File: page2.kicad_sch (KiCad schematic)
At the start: 74 parts, among them SW28 SRBV141404

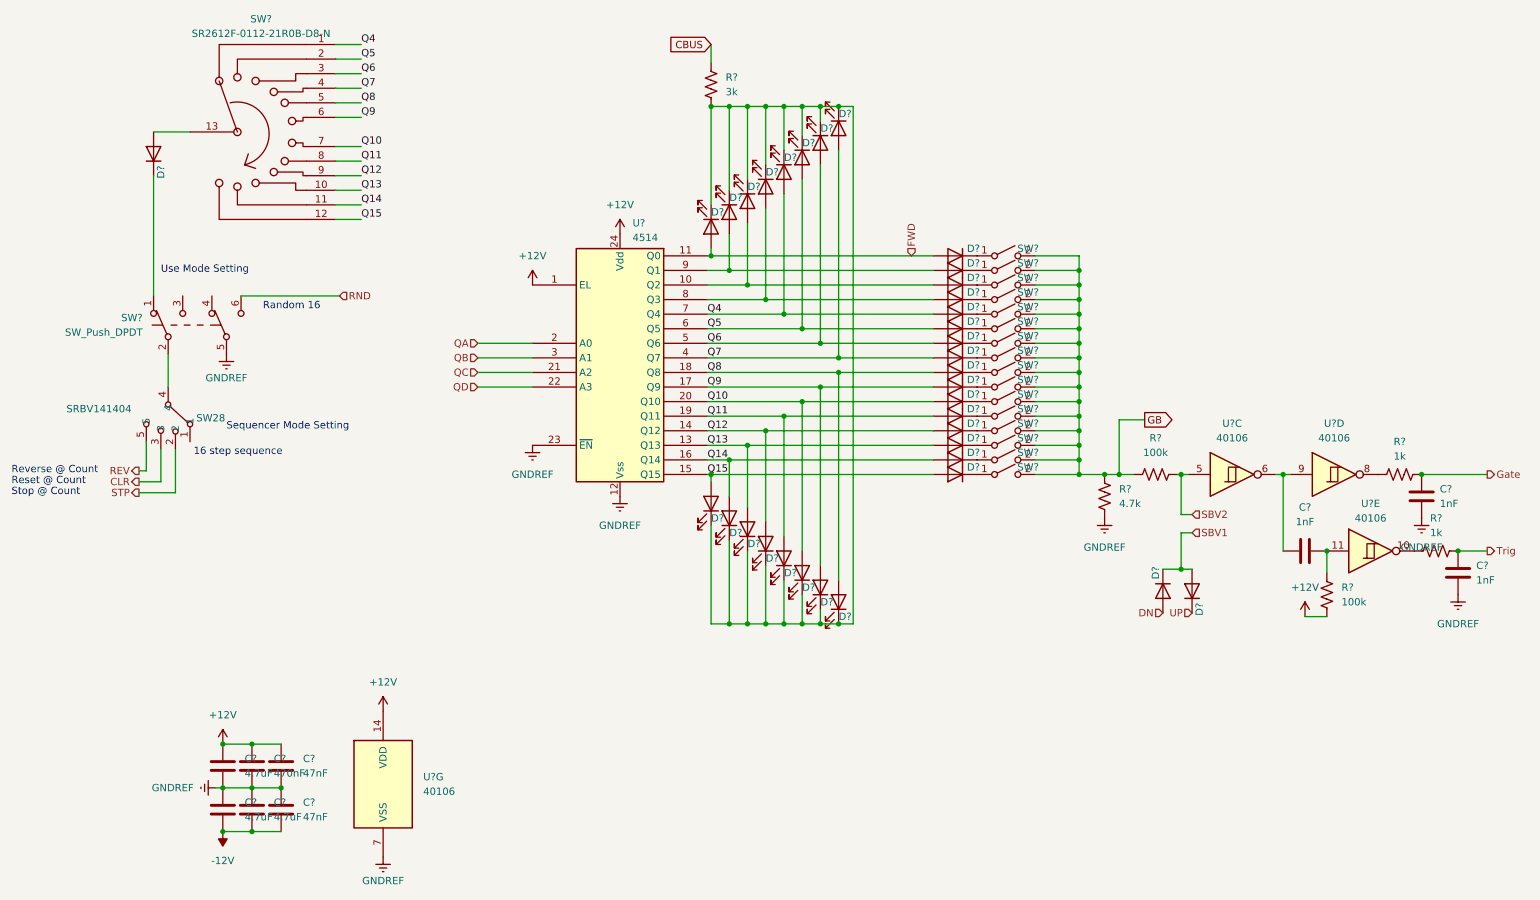
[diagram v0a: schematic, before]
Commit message: created pcb file, placed parts
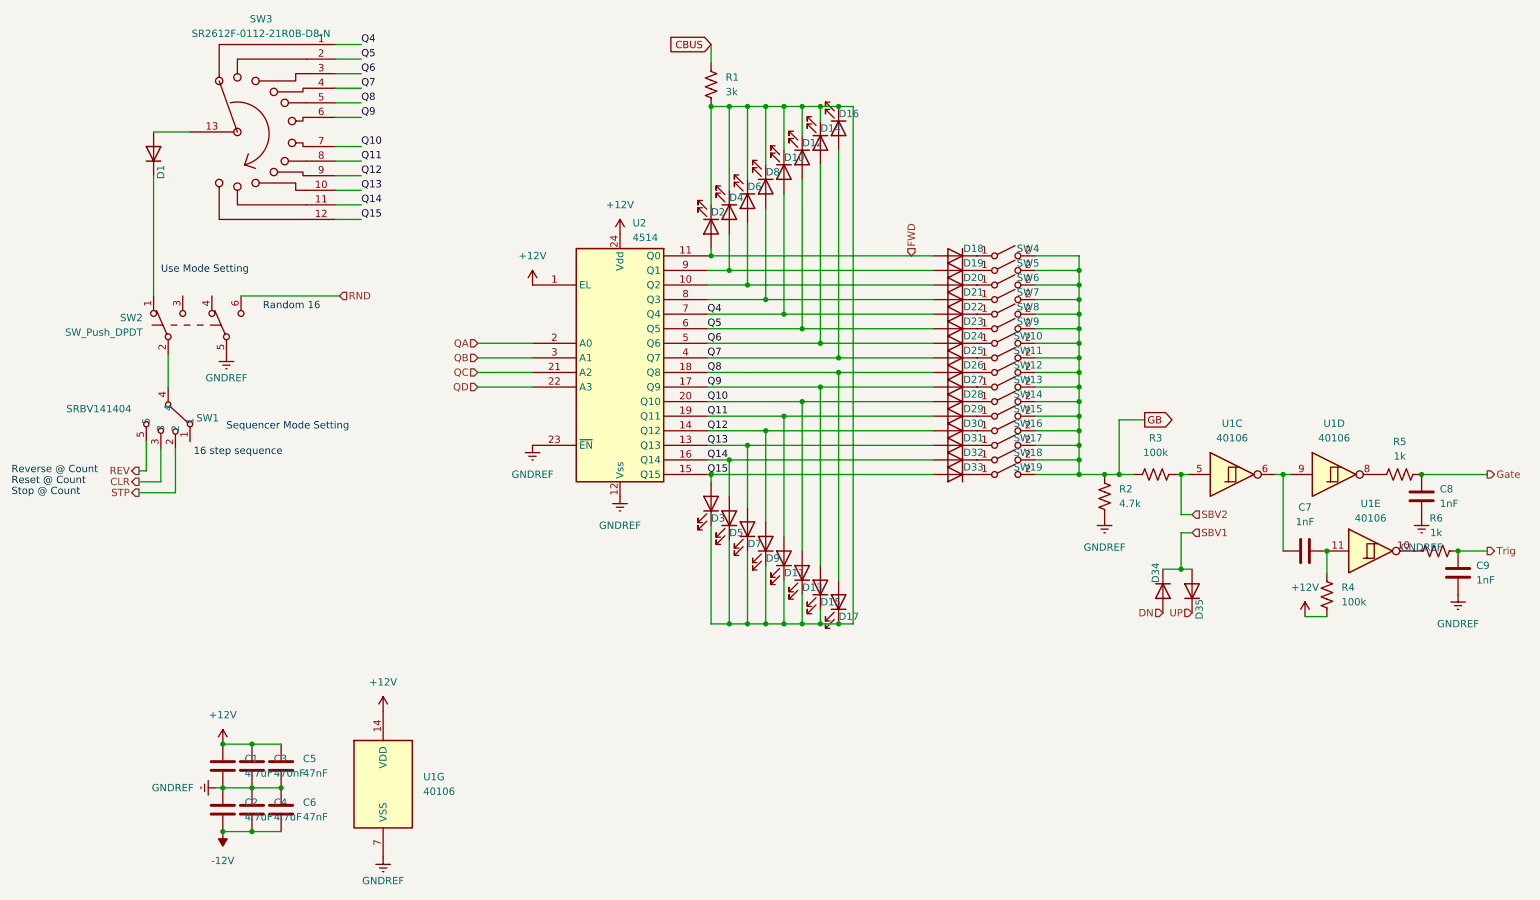
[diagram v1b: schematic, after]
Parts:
- gave numbers to parts that had none: 70
- renumbered SW28 to SW1

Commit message: routing and placing
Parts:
- D10, D11, D12, D13, D14, D15, D16, D17, D2, D3, D4, D5, D6, D7, D8, D9: footprint LED_SMD:LED_0805_2012Metric -> LED_THT:LED_D5.0mm
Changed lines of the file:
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@@
       (effects (font (size 1.27 1.27)) (justify left) hide)
     )
-    (property "Footprint" "LED_SMD:LED_0805_2012Metric" (at 140.97 109.22 0)
+    (property "Footprint" "LED_THT:LED_D5.0mm" (at 140.97 109.22 0)
       (effects (font (size 1.27 1.27)) hide)
     )
@@
       (effects (font (size 1.27 1.27)) (justify left) hide)
     )
-    (property "Footprint" "LED_SMD:LED_0805_2012Metric" (at 137.795 53.975 0)
+    (property "Footprint" "LED_THT:LED_D5.0mm" (at 137.795 53.975 0)
       (effects (font (size 1.27 1.27)) hide)
     )
@@
       (effects (font (size 1.27 1.27)) (justify left) hide)
     )
-    (property "Footprint" "LED_SMD:LED_0805_2012Metric" (at 147.32 114.3 0)
+    (property "Footprint" "LED_THT:LED_D5.0mm" (at 147.32 114.3 0)
       (effects (font (size 1.27 1.27)) hide)
     )
@@
       (effects (font (size 1.27 1.27)) (justify left) hide)
     )
-    (property "Footprint" "LED_SMD:LED_0805_2012Metric" (at 150.495 44.45 0)
+    (property "Footprint" "LED_THT:LED_D5.0mm" (at 150.495 44.45 0)
       (effects (font (size 1.27 1.27)) hide)
     )
@@
       (effects (font (size 1.27 1.27)) (justify left) hide)
     )
-    (property "Footprint" "LED_SMD:LED_0805_2012Metric" (at 153.67 119.38 0)
+    (property "Footprint" "LED_THT:LED_D5.0mm" (at 153.67 119.38 0)
       (effects (font (size 1.27 1.27)) hide)
     )
@@
       (effects (font (size 1.27 1.27)) (justify left) hide)
     )
-    (property "Footprint" "LED_SMD:LED_0805_2012Metric" (at 144.145 111.76 0)
+    (property "Footprint" "LED_THT:LED_D5.0mm" (at 144.145 111.76 0)
       (effects (font (size 1.27 1.27)) hide)
     )
@@
       (effects (font (size 1.27 1.27)) (justify left) hide)
     )
-    (property "Footprint" "LED_SMD:LED_0805_2012Metric" (at 153.67 41.91 0)
+    (property "Footprint" "LED_THT:LED_D5.0mm" (at 153.67 41.91 0)
       (effects (font (size 1.27 1.27)) hide)
     )
@@
       (effects (font (size 1.27 1.27)) (justify left) hide)
     )
-    (property "Footprint" "LED_SMD:LED_0805_2012Metric" (at 140.97 52.07 0)
+    (property "Footprint" "LED_THT:LED_D5.0mm" (at 140.97 52.07 0)
       (effects (font (size 1.27 1.27)) hide)
     )
@@
       (effects (font (size 1.27 1.27)) (justify left) hide)
     )
-    (property "Footprint" "LED_SMD:LED_0805_2012Metric" (at 134.62 56.515 0)
+    (property "Footprint" "LED_THT:LED_D5.0mm" (at 134.62 56.515 0)
       (effects (font (size 1.27 1.27)) hide)
     )
@@
       (effects (font (size 1.27 1.27)) (justify left) hide)
     )
-    (property "Footprint" "LED_SMD:LED_0805_2012Metric" (at 156.845 121.92 0)
+    (property "Footprint" "LED_THT:LED_D5.0mm" (at 156.845 121.92 0)
       (effects (font (size 1.27 1.27)) hide)
     )
@@
       (effects (font (size 1.27 1.27)) (justify left) hide)
     )
-    (property "Footprint" "LED_SMD:LED_0805_2012Metric" (at 156.845 39.37 0)
+    (property "Footprint" "LED_THT:LED_D5.0mm" (at 156.845 39.37 0)
       (effects (font (size 1.27 1.27)) hide)
     )
@@
       (effects (font (size 1.27 1.27)) (justify left) hide)
     )
-    (property "Footprint" "LED_SMD:LED_0805_2012Metric" (at 150.495 116.84 0)
+    (property "Footprint" "LED_THT:LED_D5.0mm" (at 150.495 116.84 0)
       (effects (font (size 1.27 1.27)) hide)
     )
@@
       (effects (font (size 1.27 1.27)) (justify left) hide)
     )
-    (property "Footprint" "LED_SMD:LED_0805_2012Metric" (at 137.795 107.315 0)
+    (property "Footprint" "LED_THT:LED_D5.0mm" (at 137.795 107.315 0)
       (effects (font (size 1.27 1.27)) hide)
     )
@@
       (effects (font (size 1.27 1.27)) (justify left) hide)
     )
-    (property "Footprint" "LED_SMD:LED_0805_2012Metric" (at 144.145 49.53 0)
+    (property "Footprint" "LED_THT:LED_D5.0mm" (at 144.145 49.53 0)
       (effects (font (size 1.27 1.27)) hide)
     )
@@
       (effects (font (size 1.27 1.27)) (justify left) hide)
     )
-    (property "Footprint" "LED_SMD:LED_0805_2012Metric" (at 134.62 104.775 0)
+    (property "Footprint" "LED_THT:LED_D5.0mm" (at 134.62 104.775 0)
       (effects (font (size 1.27 1.27)) hide)
     )
@@
       (effects (font (size 1.27 1.27)) (justify left) hide)
     )
-    (property "Footprint" "LED_SMD:LED_0805_2012Metric" (at 147.32 46.99 0)
+    (property "Footprint" "LED_THT:LED_D5.0mm" (at 147.32 46.99 0)
       (effects (font (size 1.27 1.27)) hide)
     )

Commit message: routed 100%
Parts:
- removed C1, C2, C4: 4.7uF, Capacitor_SMD:C_0805_2012Metric, symbol Device:C
- removed C3: 470nF, Capacitor_SMD:C_0805_2012Metric, symbol Device:C
- removed C5, C6: 47nF, Capacitor_SMD:C_0603_1608Metric, symbol Device:C
- added C52 (x2): 470nF, Capacitor_SMD:C_0805_2012Metric, symbol Device:C
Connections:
- net +12V: now also C52.1, C52.1
- net GNDREF: now also C52.2, C52.2
